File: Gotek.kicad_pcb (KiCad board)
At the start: 2 copper layers, 111.6 x 59.4 mm, 68 parts, among them J4 M20-8760542P, J5 M20-8760442, J7 OLED, J8 RotaryEncoder, P1 2005280260, P3 USB_A, Q1 PMBT2222A,215, Q2 PMBT2222A,215, Q3 PMBT2222A,215, Q4 PMBT2222A,215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

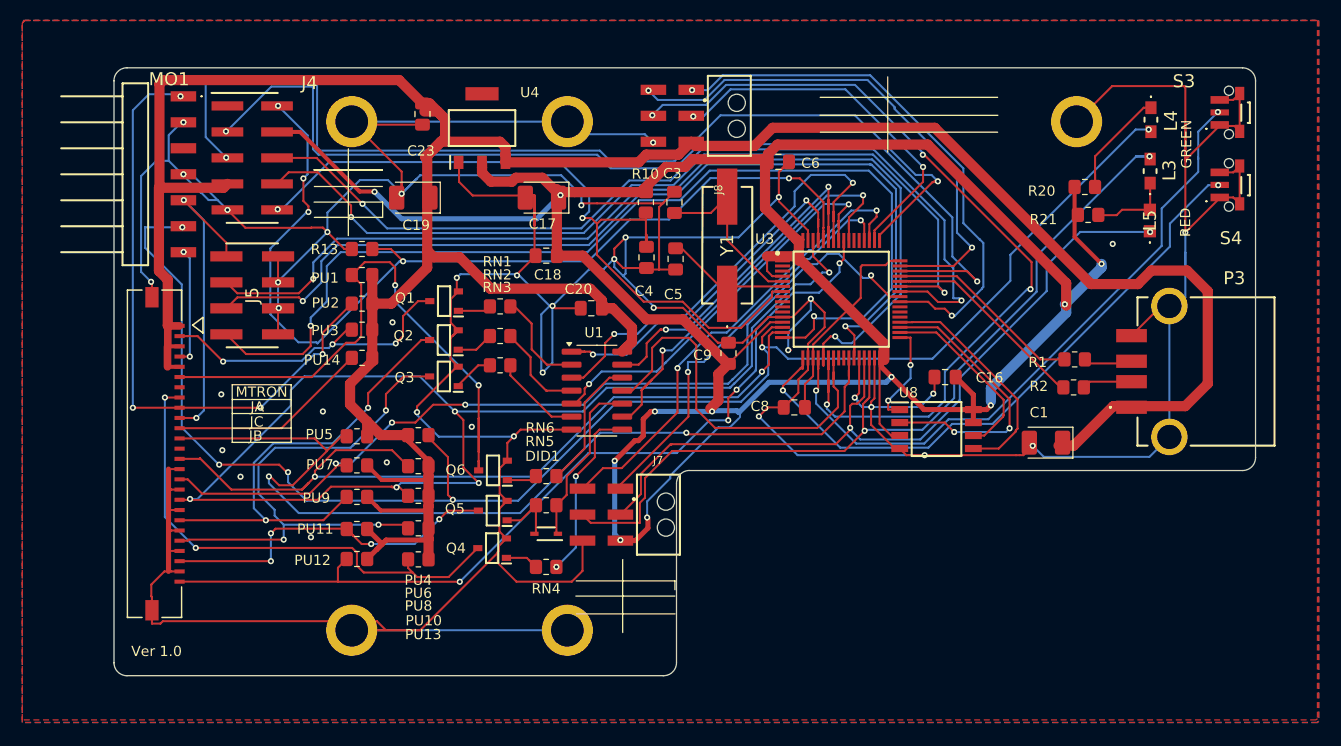
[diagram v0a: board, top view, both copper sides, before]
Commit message: Add files via upload
Schematic and gerbers for a Gotek(?) compatible with an Artery AT32F435RGT7 chip and a 26 Pin FFC connector.
Used SFRKC30.AT4.35 PCB for most of the schematic and layout but used SFRC2D.B PCB for the 26 Pin FFC connections.
Used photographs and a multimeter along with removing U1 and U3 on the SFRKC30.AT4.35 to get to the traces underneath.
Where possible I followed the original PCB routing of the SFRKC30.AT4.35 but Kicad has some different rules for trace widths (between pins 5&6 of U8 which isn't fitted).
Removed L3 Green LED and changed R21 to 12K to reduce it's brightness. Also increased the pad sizes for the diode D1D to make it easier to hand solder. Minor changes to silk screen.
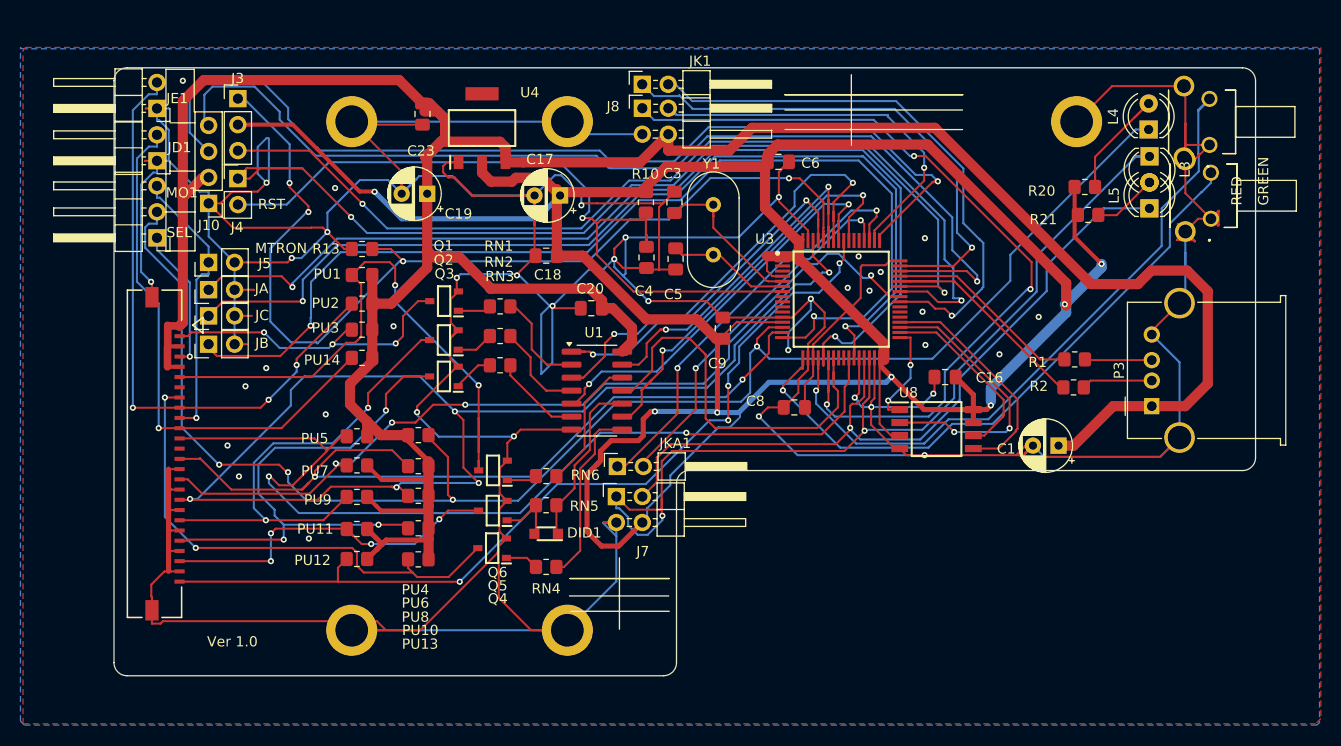
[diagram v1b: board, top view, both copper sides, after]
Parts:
- added J10: Conn_01x04_Pin, Connector_PinHeader_2.54mm:PinHeader_1x04_P2.54mm_Vertical, F.Cu at (104.5, 68.6)
- added J3: Conn_01x03_Pin, Connector_PinHeader_2.54mm:PinHeader_1x03_P2.54mm_Vertical, F.Cu at (107.4, 58.4)
- added JA1: Conn_01x02, Connector_PinHeader_2.54mm:PinHeader_1x02_P2.54mm_Vertical, F.Cu at (104.5, 77.1)
- added JB1: Conn_01x02, Connector_PinHeader_2.54mm:PinHeader_1x02_P2.54mm_Vertical, F.Cu at (104.5, 82.4)
- added JC1: Conn_01x02, Connector_PinHeader_2.54mm:PinHeader_1x02_P2.54mm_Vertical, F.Cu at (104.5, 79.6)
- added JD1: Conn_01x02_Pin, Connector_PinHeader_2.54mm:PinHeader_1x02_P2.54mm_Horizontal, F.Cu at (99.5, 64.5)
- added JE1: Conn_01x02_Pin, Connector_PinHeader_2.54mm:PinHeader_1x02_P2.54mm_Horizontal, F.Cu at (99.5, 59.4)
- added JK1: Conn_01x02, Connector_PinHeader_2.54mm:PinHeader_2x01_P2.54mm_Horizontal, F.Cu at (146.9, 57.0)
- added JKA1: Conn_01x02, Connector_PinHeader_2.54mm:PinHeader_2x01_P2.54mm_Horizontal, F.Cu at (144.5, 94.4)
- C1, C17, C19: value 47uF -> 100uF; footprint Capacitor_Tantalum_SMD:CP_EIA-3528-21_Kemet-B_Pad1.50x2.35mm_HandSolder -> Capacitor_THT:CP_Radial_D5.0mm_P2.50mm
- J4: value M20-8760542P -> Conn_01x02_Pin; footprint Gotek:HUSSP10W64P254_2X5_1270X500X1043P -> Connector_PinHeader_2.54mm:PinHeader_1x02_P2.54mm_Vertical
- J5: value M20-8760442 -> Conn_01x02; footprint Gotek:M208760442 -> Connector_PinHeader_2.54mm:PinHeader_1x02_P2.54mm_Vertical
- J7, J8: footprint Gotek:610106249121 -> Connector_PinHeader_2.54mm:PinHeader_2x02_P2.54mm_Horizontal
- L3, L4: footprint Gotek:APT2012PGW -> LED_THT:LED_D4.0mm
- L5: footprint Gotek:HSMCC177 -> LED_THT:LED_D4.0mm
- MO1: footprint Gotek:M208900705 -> Connector_PinHeader_2.54mm:PinHeader_1x03_P2.54mm_Horizontal
- P3: footprint Gotek:USB1046GF0190LBA -> Connector_USB:USB_A_Molex_67643_Horizontal
- R21: value 1K -> 12K
- S3, S4: value SKRTLAE010 -> SKHHANA010; footprint Gotek:SKRTLAE010 -> Gotek:SKHHLQA010
- Y1: footprint Gotek:LFXTAL050985Bulk -> Crystal:Crystal_HC18-U_Vertical
- moved J8 9.26 mm to (146.9, 59.3), turned to 0 degrees
- moved MO1 7.08 mm to (99.5, 72.0), turned to 180 degrees
- moved P3 6.29 mm to (196.7, 88.5)
- moved J5 5.34 mm to (104.5, 74.4), turned to 90 degrees
- moved J7 5.16 mm to (144.4, 97.3), turned to 0 degrees
- moved S4 3.92 mm to (202.5, 70.1)
- moved S3 3.89 mm to (202.3, 62.9)
- moved C9 2.52 mm to (154.8, 80.8)
- moved J4 2.46 mm to (107.4, 66.2), turned to 0 degrees
- moved C17 1.79 mm to (138.9, 67.9)
- moved Y1 1.65 mm to (153.8, 73.7)
- moved L3 1.44 mm to (196.5, 64.0), turned to -90 degrees
- moved C19 1.41 mm to (125.9, 67.7)
- moved C1 1.26 mm to (187.6, 92.3)
- moved L5 1.19 mm to (196.5, 69.1), turned to 90 degrees
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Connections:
- net D+ renamed Net-(P3-D+)
- net D- renamed Net-(P3-D-)
- J4 pad 1: unconnected-(J4-Pad1) -> USART1_RX
- J4 pad 2: J3_BOOT0 -> NRST
- J7 pad 1: JKA1-2 -> /I2C2_CLK
- J7 pad 2: JKA1-1 -> /I2C2_DTA
- J7 pad 3: I2C2_DTA -> GND
- J7 pad 4: I2C2_CLK -> +3.3V
- J8 pad 1: U3-40-PC9 -> ENC1
- J8 pad 2: ENCSW -> ENC2
- J8 pad 3: ENC2 -> GND
- J8 pad 4: ENC1 -> 5V
- L3 pad 1: Net-(L3-A) -> /I2C2_CLK
- L3 pad 2: I2C2_CLK -> Net-(L3-A)
- L4 pad 1: Net-(L4-A) -> SEL
- L4 pad 2: SEL -> Net-(L4-A)
- L5 pad 1: I2C2_DTA -> /I2C2_DTA
- MO1 pad 1: HDOUT -> DRVSEL
- MO1 pad 2: GND -> SEL
- MO1 pad 3: DINST -> MTRON
- P1 pad 11: Net-(P1-Pad11) -> DINST
- PU14 pad 1: Net-(P1-Pad11) -> DINST
- U3 pad 29: I2C2_DTA -> /I2C2_DTA
- U3 pad 30: I2C2_CLK -> /I2C2_CLK
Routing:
- net /I2C2_CLK: track 0.00 -> 92.1 mm, vias 0 -> 2
- net I2C2_CLK: track 85.3 -> 0.00 mm, vias 2 -> 0
- net I2C2_DTA: track 76.0 -> 0.00 mm, vias 2 -> 0
- net /I2C2_DTA: track 0.00 -> 74.3 mm, vias 0 -> 1
- net GND: track 605.8 -> 665.1 mm, vias 38 -> 39
- net DINST: track 0.00 -> 52.6 mm, vias 0 -> 1
- net Net-(P1-Pad11): track 19.7 -> 0.00 mm
- net +3.3V: track 321.9 -> 339.2 mm, vias 11 -> 7
- net USART1_RX: track 86.0 -> 96.8 mm
- net USART1_TX: track 89.6 -> 94.3 mm
- net JKA1-1: track 46.7 -> 42.5 mm
- net SWCLK: track 100.3 -> 96.3 mm, vias 2 -> 1
- net BUT_R: track 64.7 -> 68.7 mm, vias 2 -> 1
- net MTRON: track 31.3 -> 27.5 mm, vias 2 -> 1
- net JKA1-2: track 39.9 -> 36.2 mm
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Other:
- board text added: "RST"
- board text added: "SEL"
